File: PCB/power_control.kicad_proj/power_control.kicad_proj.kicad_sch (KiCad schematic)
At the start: 14 parts, among them J1 5V, J2 GND, J3 PWR LED, J4 HDD LED, J5 PWR SW, J6 RST SW, J7 ESP32_1, J8 ESP32_2, SW1 PWR, SW2 RST

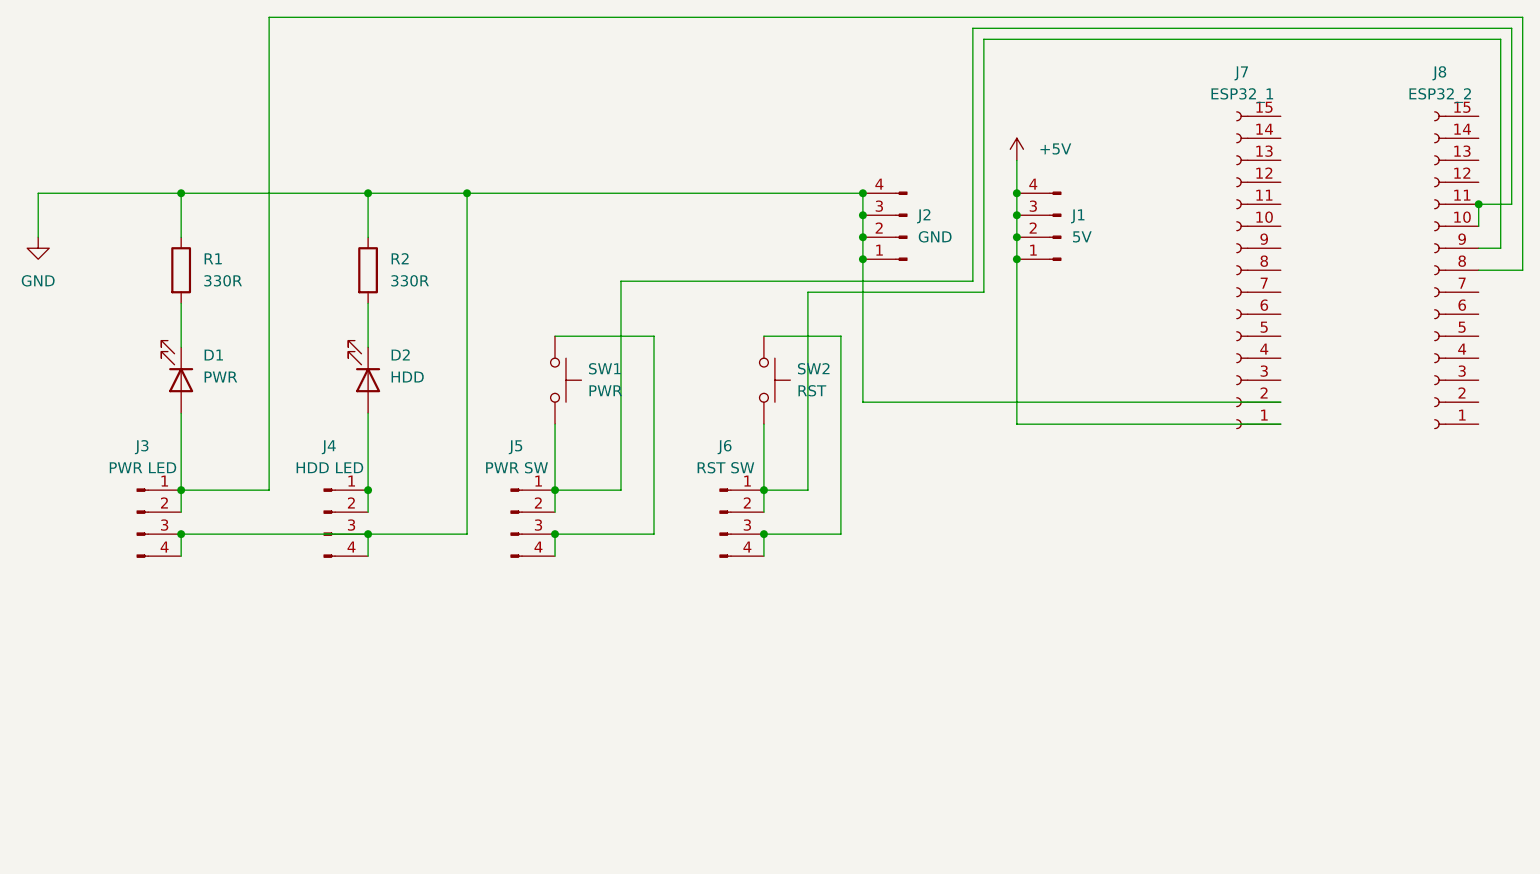
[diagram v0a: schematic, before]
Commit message: Major rework of PCB, incompatible!
use transistors to sense LED and switch pins
add system header compatible with mainboard header
move pins to one side -> only single header required
we now need two PCB sides, yay
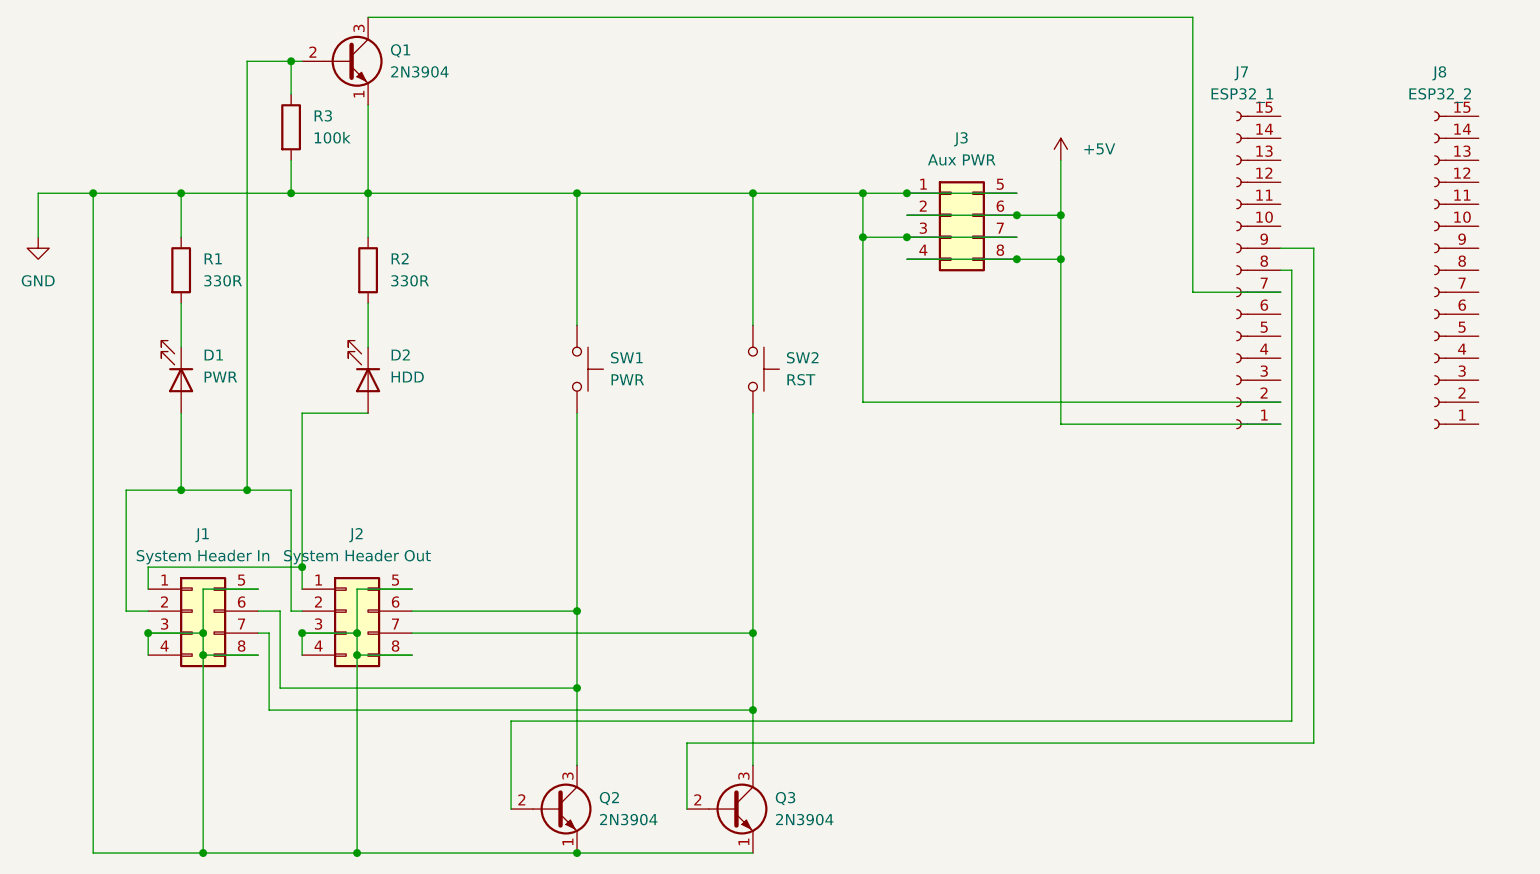
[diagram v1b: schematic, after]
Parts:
- removed J1: 5V, Connector_PinHeader_2.54mm:PinHeader_1x04_P2.54mm_Vertical, symbol Connector:Conn_01x04_Pin
- removed J2: GND, Connector_PinHeader_2.54mm:PinHeader_1x04_P2.54mm_Vertical, symbol Connector:Conn_01x04_Pin
- removed J3: PWR LED, Connector_PinHeader_2.54mm:PinHeader_1x04_P2.54mm_Vertical, symbol Connector:Conn_01x04_Pin
- removed J4: HDD LED, Connector_PinHeader_2.54mm:PinHeader_1x04_P2.54mm_Vertical, symbol Connector:Conn_01x04_Pin
- removed J5: PWR SW, Connector_PinHeader_2.54mm:PinHeader_1x04_P2.54mm_Vertical, symbol Connector:Conn_01x04_Pin
- removed J6: RST SW, Connector_PinHeader_2.54mm:PinHeader_1x04_P2.54mm_Vertical, symbol Connector:Conn_01x04_Pin
- added J1: System Header In, Connector_PinHeader_2.54mm:PinHeader_2x04_P2.54mm_Vertical, symbol Connector_Generic:Conn_02x04_Top_Bottom
- added J2: System Header Out, Connector_PinHeader_2.54mm:PinHeader_2x04_P2.54mm_Vertical, symbol Connector_Generic:Conn_02x04_Top_Bottom
- added J3: Aux PWR, Connector_PinHeader_2.54mm:PinHeader_2x04_P2.54mm_Vertical, symbol Connector_Generic:Conn_02x04_Top_Bottom
- added Q1, Q2, Q3: 2N3904, Package_TO_SOT_THT:TO-92_Inline, symbol Transistor_BJT:2N3904
- added R3: 100k, Resistor_THT:R_Axial_DIN0207_L6.3mm_D2.5mm_P10.16mm_Horizontal, symbol Device:R
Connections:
- net +5V: now also J3.2 (5V), J3.4 (5V), J3.6 (5V), J3.8 (5V)
- net GND: now also SW1.1, SW2.1, J1.3 (GND), J1.4 (GND), J1.5 (GND), J1.8 (GND), J2.3 (GND), J2.4 (GND), J2.5 (GND), J2.8 (GND), J3.1 (GND), J3.3 (GND), J3.5 (GND), J3.7 (GND), Q1.1 (E), Q2.1 (E), Q3.1 (E), R3.2
- net at D2.2 (A): now also J1.1 (HDD+), J2.1 (HDD+)
- net at D1.2 (A): now also J1.2 (PWR_LED+), J2.2 (PWR_LED+), Q1.2 (B), R3.1; no longer J8.8 (Pin_8)
- net at J7.7 (D26): now also Q1.3 (C)
- net at J7.8 (D25): now also Q2.2 (B)
- net at J7.9 (D33): now also Q3.2 (B)
- net at SW2.2: now also J1.7 (RST+), J2.7 (RST+), Q3.3 (C); no longer J8.9 (Pin_9)
- new net: J1.6 (PWR_BTN+), J2.6 (PWR_BTN+), Q2.3 (C), SW1.2
- now unconnected: J8.10 (Pin_10), J8.11 (Pin_11)
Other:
- moved on the sheet: SW1, SW2
